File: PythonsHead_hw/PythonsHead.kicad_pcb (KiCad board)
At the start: 2 copper layers, 45 x 45 mm, 92 parts, among them Q1 MMBT2222, Q2 MMBT2222, Q3 MMBT2222, Q4 MMBT2222, Q5 MMBT2222, Q6 MMBT2222, Q7 MMBT2222, Q8 MMBT2222

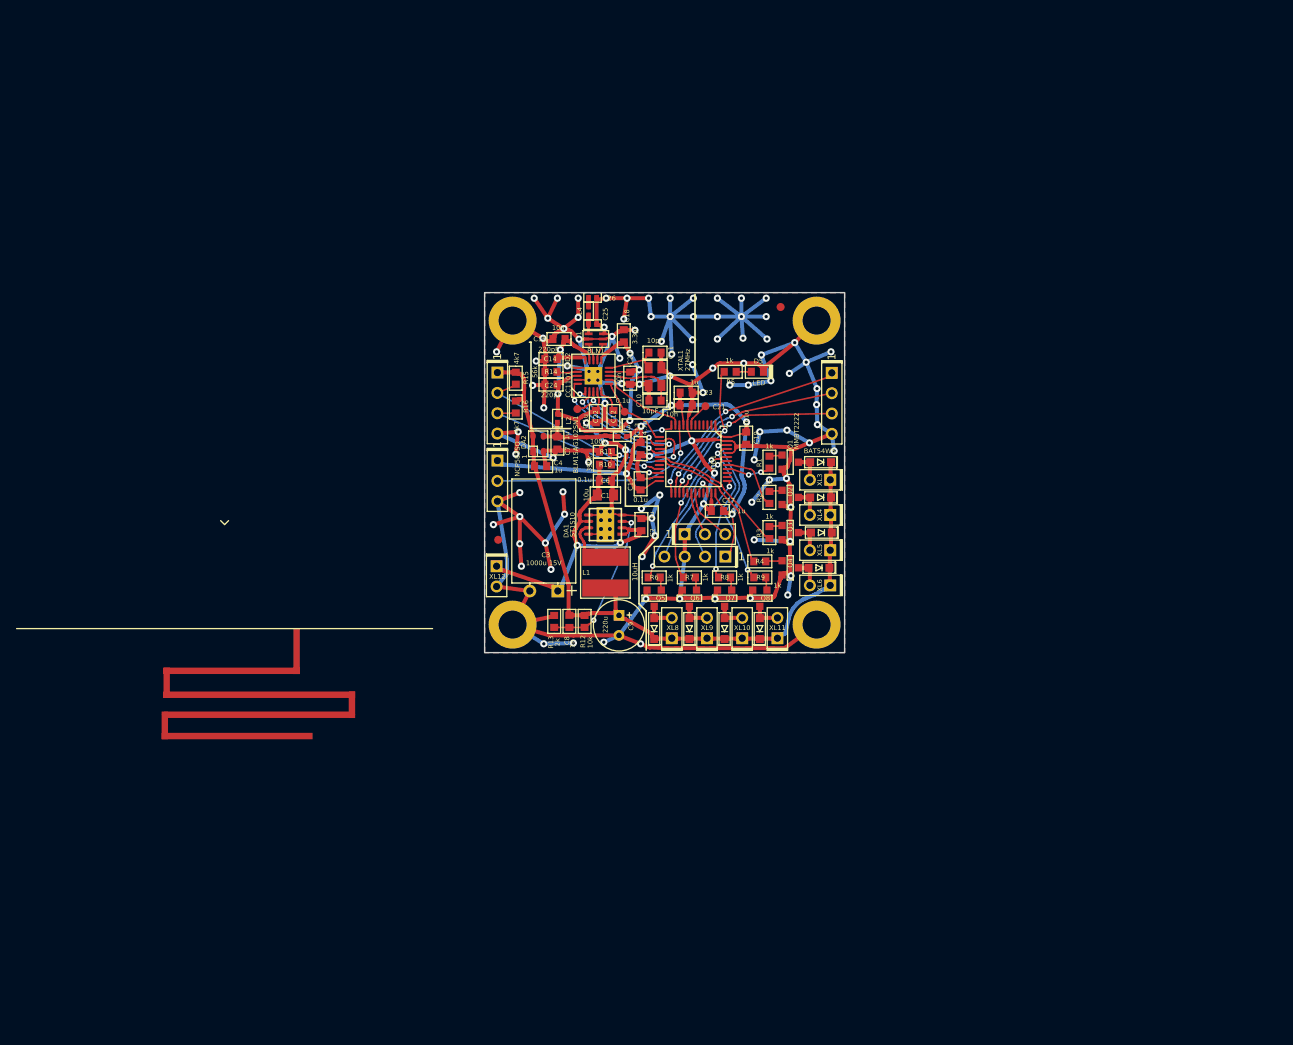
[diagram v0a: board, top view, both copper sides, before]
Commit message: * HW done + FW radio init
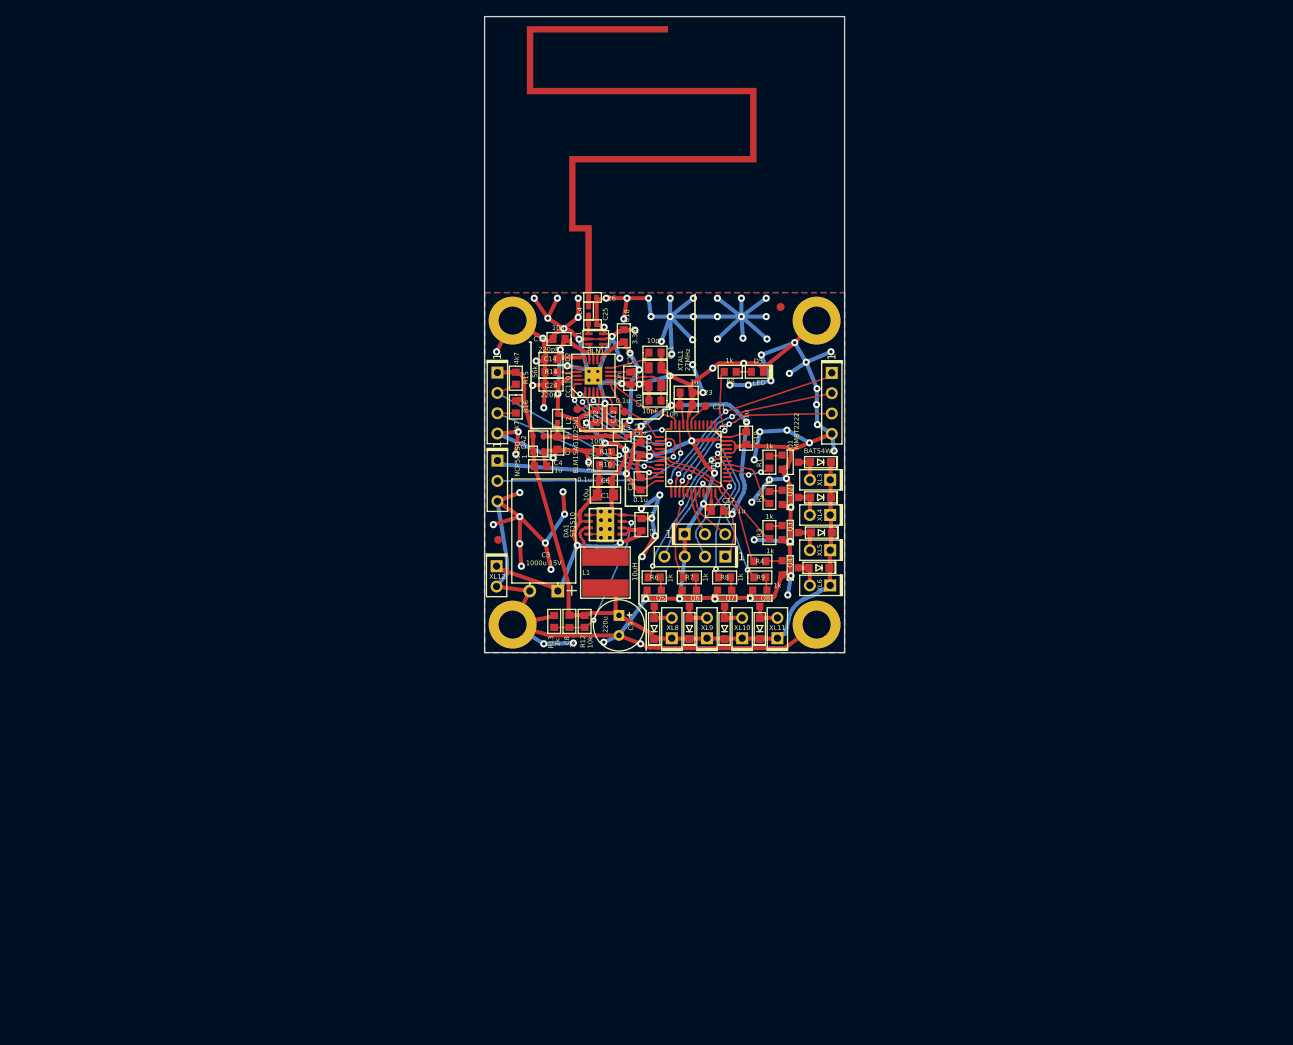
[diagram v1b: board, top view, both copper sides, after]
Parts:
- ANT1: footprint Radio:ANT_868_ROUND_MEANDER -> Radio:ANT_868_MEANDER_4HOR_45mm
- moved ANT1 69.2 mm to (114.5, 54.0), turned to 180 degrees
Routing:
- net /ANT2: track 1.20 -> 6.02 mm
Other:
- board size 45 x 45 mm -> 45 x 79.5 mm
- net class Ant added: clearance 0.2, trace_width 0.6, via_dia 0.7, via_drill 0.3
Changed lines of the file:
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@@
   (general
     (links 214)
-    (no_connects 8)
-    (area 32.488919 52.655 137.97363 112.775001)
+    (no_connects 7)
+    (area 91.924999 53.924999 137.075001 99.075001)
     (thickness 1.6)
-    (drawings 28)
-    (tracks 2345)
+    (drawings 30)
+    (tracks 2346)
     (zones 0)
     (modules 92)
@@
   (page A4)
   (layers
-    (0 F.Cu signal hide)
-    (31 B.Cu signal hide)
+    (0 F.Cu signal)
+    (31 B.Cu signal)
     (36 B.SilkS user)
     (37 F.SilkS user)
@@
     (40 Dwgs.User user)
     (44 Edge.Cuts user)
+    (49 F.Fab user hide)
   )
   (setup
@@
     (uvia_dia 0.3)
     (uvia_drill 0.1)
-    (add_net /ANT1)
-    (add_net /ANT2)
     (add_net /BAT_MEAS)
     (add_net /CC_CS)
@@
     (add_net "Net-(Q8-Pad1)")
   )
+  (net_class Ant ""
+    (clearance 0.2)
+    (trace_width 0.6)
+    (via_dia 0.7)
+    (via_drill 0.3)
+    (uvia_dia 0.3)
+    (uvia_drill 0.1)
+    (add_net /ANT1)
+    (add_net /ANT2)
+  )
   (net_class Wide ""
     (clearance 0.2)
@@
     (add_net VCC)
   )
-  (module Radio:ANT_868_ROUND_MEANDER (layer F.Cu)
-    (at 59.5 96)
-    (descr "Meander antenna for circular PCB R=29.5")
-    (fp_text reference ANT1 (at -7.4 1) (layer F.SilkS) hide
-      (effects (font (size 0.6 0.6) (thickness 0.15)))
-    )
-    (fp_text value ANT_PCB_MONO (at -8.2 2.6) (layer F.Fab) hide
-      (effects (font (size 0.6 0.6) (thickness 0.15)))
-    )
-    (fp_circle (center -20.5 2.5) (end -20.5 -0.5) (layer Dwgs.User) (width 0.15))
-    (fp_line (start 26 0) (end -26 0) (layer F.SilkS) (width 0.15))
-    (fp_arc (start 0 -13) (end 0 16.5) (angle 65) (layer Dwgs.User) (width 0.15))
-    (fp_arc (start 0 -13) (end 0 16.5) (angle -65) (layer Dwgs.User) (width 0.15))
-    (fp_line (start -0.5 -13.5) (end 0 -13) (layer F.SilkS) (width 0.15))
-    (fp_line (start 0.5 -13.5) (end 0 -13) (layer F.SilkS) (width 0.15))
-    (pad 1 smd rect (at 0.88 5.28 180) (size 17.04 0.8) (layers F.Cu)
-      (net 1 /ANT2))
-    (pad 1 smd rect (at -7.24 6.775 180) (size 0.8 3.79) (layers F.Cu)
-      (net 1 /ANT2))
-    (pad 1 smd rect (at 15.92 9.525 180) (size 0.8 3.31) (layers F.Cu)
-      (net 1 /ANT2))
-    (pad 1 smd rect (at 4.34 8.27 180) (size 23.96 0.8) (layers F.Cu)
-      (net 1 /ANT2))
-    (pad 1 smd rect (at 1.565 13.43 180) (size 18.87 0.8) (layers F.Cu)
-      (net 1 /ANT2))
-    (pad 1 smd oval (at 4.23 10.77 180) (size 24.18 0.8) (layers F.Cu)
-      (net 1 /ANT2))
-    (pad 1 smd rect (at -7.47 12.1 180) (size 0.8 3.46) (layers F.Cu)
-      (net 1 /ANT2))
-    (pad 1 smd rect (at 9 2.84 180) (size 0.8 5.68) (layers F.Cu)
-      (net 1 /ANT2))
-  )
   (module Radio:BALUN_JOHANSON868 (layer F.Cu)
     (at 105.9 59.8 90)
@@
     )
   )
+  (module Radio:ANT_868_MEANDER_4HOR_45mm (layer F.Cu)
+    (at 114.5 54 180)
+    (fp_text reference ANT1 (at 0 -2.5 180) (layer F.SilkS) hide
+      (effects (font (size 1 1) (thickness 0.15)))
+    )
+    (fp_text value ANT_PCB_MONO (at 0 -1 180) (layer F.SilkS) hide
+      (effects (font (size 1 1) (thickness 0.15)))
+    )
+    (fp_line (start -22.5 0) (end 22.5 0) (layer F.Fab) (width 0.15))
+    (fp_line (start 22.5 0) (end 22.5 34.5) (layer F.Fab) (width 0.15))
+    (fp_line (start 22.5 34.5) (end -22.5 34.5) (layer F.Fab) (width 0.15))
+    (fp_line (start -22.5 34.5) (end -22.5 0) (layer F.Fab) (width 0.15))
+    (pad 1 smd rect (at 9.5 4.215 180) (size 0.8 8.43) (layers F.Cu)
+      (net 1 /ANT2))
+    (pad 1 smd rect (at 10.515 8.03 180) (size 1.23 0.8) (layers F.Cu)
+      (net 1 /ANT2))
+    (pad 1 smd rect (at 11.53 12.35 180) (size 0.8 9.44) (layers F.Cu)
+      (net 1 /ANT2))
+    (pad 1 smd rect (at 0.22 16.67 180) (size 21.82 0.8) (layers F.Cu)
+      (net 1 /ANT2))
+    (pad 1 smd rect (at -11.09 20.93 180) (size 0.8 9.32) (layers F.Cu)
+      (net 1 /ANT2))
+    (pad 1 smd rect (at 2.865 25.19 180) (size 27.11 0.8) (layers F.Cu)
+      (net 1 /ANT2))
+    (pad 1 smd rect (at 16.82 29.045 180) (size 0.8 8.51) (layers F.Cu)
+      (net 1 /ANT2))
+    (pad 1 smd rect (at 8 32.91 180) (size 16.84 0.8) (layers F.Cu)
+      (net 1 /ANT2))
+  )
+  (gr_line (start 137 19.5) (end 137 54) (angle 90) (layer Edge.Cuts) (width 0.15))
+  (gr_line (start 92 19.5) (end 137 19.5) (angle 90) (layer Edge.Cuts) (width 0.15))
+  (gr_line (start 92 54) (end 92 19.5) (angle 90) (layer Edge.Cuts) (width 0.15))
   (gr_line (start 112.2 93.8) (end 112.2 98.7) (angle 90) (layer F.SilkS) (width 0.2))
   (gr_line (start 111.3 92.9) (end 112.2 93.8) (angle 90) (layer F.SilkS) (width 0.2))
@@
   (gr_line (start 137 99) (end 92 99) (angle 90) (layer Edge.Cuts) (width 0.15))
   (gr_line (start 137 54) (end 137 99) (angle 90) (layer Edge.Cuts) (width 0.15))
-  (gr_line (start 92 54) (end 137 54) (angle 90) (layer Edge.Cuts) (width 0.15))
+  (segment (start 105 54.6) (end 105 49.785) (width 0.6) (layer F.Cu) (net 1) (status C00000))
   (segment (start 105 54.9) (end 105 54.6) (width 0.6) (layer F.Cu) (net 1))
   (segment (start 105 55.5) (end 105 54.9) (width 0.6) (layer F.Cu) (net 1))
@@
   (segment (start 127.289 91.184) (end 127.2195 90.8268) (width 0.2) (layer F.Cu) (net 60))
   (zone (net 3) (net_name GND) (layer F.Cu) (hatch edge 0.508)
-    (connect_pads (clearance 0.3))
+    (connect_pads yes (clearance 0.3))
     (min_thickness 0.254)
     (fill yes (arc_segments 32) (thermal_gap 0.3) (thermal_bridge_width 0.3))
@@
   )
   (zone (net 3) (net_name GND) (layer B.Cu) (hatch edge 0.508)
-    (connect_pads (clearance 0.3))
+    (connect_pads yes (clearance 0.3))
     (min_thickness 0.254)
     (fill yes (arc_segments 32) (thermal_gap 0.3) (thermal_bridge_width 0.3))

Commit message: Layout done
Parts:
- removed C14: 220pF, Capacitors:CAP_0603
- removed XL13: CONN_3, Connectors:PLS-3
- added C27: 18pF, Capacitors:CAP_0603, F.Cu at (115.4, 85.0)
- added C28: 10n, Capacitors:CAP_0603, F.Cu at (105.4, 83.6)
- added C29: 0.1u, Capacitors:CAP_0603, F.Cu at (109.6, 93.2)
- added C30: 3.3pF, Capacitors:CAP_0603, F.Cu at (111.0, 83.6)
- added C31: 10n, Capacitors:CAP_0603, F.Cu at (113.0, 88.0)
- added C32: 0.1u, Capacitors:CAP_0603, F.Cu at (108.0, 93.2)
- added C33: 220pF, Capacitors:CAP_0603, F.Cu at (102.4, 88.8)
- added C34: *, Capacitors:CAP_0402, F.Cu at (105.8, 81.6)
- added C35: *, Capacitors:CAP_0402, F.Cu at (110.2, 81.6)
- added C36: 100u, Capacitors:SMD_D6d3, F.Cu at (95.0, 108.8)
- added C37: 100u, Capacitors:SMD_D6d3, F.Cu at (111.0, 108.8)
- added C38: 100u, Capacitors:SMD_D6d3, F.Cu at (103.0, 108.8)
- added C39: 100u, Capacitors:SMD_D6d3, F.Cu at (119.0, 108.8)
- added C40: 100u, Capacitors:SMD_D6d3, F.Cu at (94.6, 124.6)
- added C41: 100u, Capacitors:SMD_D6d3, F.Cu at (110.6, 124.6)
- added C42: 100u, Capacitors:SMD_D6d3, F.Cu at (102.6, 124.6)
- added C43: 100u, Capacitors:SMD_D6d3, F.Cu at (118.6, 124.6)
- added C44: 0.1u, Capacitors:CAP_0603, F.Cu at (94.6, 130.4)
- added C45: 0.1u, Capacitors:CAP_0603, F.Cu at (110.6, 130.4)
- added C46: 0.1u, Capacitors:CAP_0603, F.Cu at (102.6, 130.4)
- added C47: 0.1u, Capacitors:CAP_0603, F.Cu at (118.6, 130.4)
- added C48: 0.1u, Capacitors:CAP_0603, B.Cu at (96.6, 131.4)
- added C49: 0.1u, Capacitors:CAP_0603, B.Cu at (112.8, 131.4)
- added C5: 0.1u, Capacitors:CAP_0603, F.Cu at (82.8, 104.5)
- added C50: 0.1u, Capacitors:CAP_0603, B.Cu at (104.6, 131.4)
- added C51: 0.1u, Capacitors:CAP_0603, B.Cu at (120.8, 131.4)
- added C52: 100u, Capacitors:SMD_D6d3, F.Cu at (127.0, 108.8)
- added C53: 100u, Capacitors:SMD_D6d3, F.Cu at (143.0, 108.8)
- added C54: 100u, Capacitors:SMD_D6d3, F.Cu at (135.0, 108.8)
- added C55: 100u, Capacitors:SMD_D6d3, F.Cu at (151.0, 108.8)
- added C56: 100u, Capacitors:SMD_D6d3, F.Cu at (126.6, 124.6)
- added C57: 100u, Capacitors:SMD_D6d3, F.Cu at (142.6, 124.6)
- added C58: 100u, Capacitors:SMD_D6d3, F.Cu at (134.6, 124.6)
- added C59: 100u, Capacitors:SMD_D6d3, F.Cu at (150.6, 124.6)
- added C60: 0.1u, Capacitors:CAP_0603, F.Cu at (126.6, 130.4)
- added C61: 0.1u, Capacitors:CAP_0603, F.Cu at (142.6, 130.4)
- added C62: 0.1u, Capacitors:CAP_0603, F.Cu at (134.6, 130.4)
- added C63: 0.1u, Capacitors:CAP_0603, F.Cu at (150.6, 130.4)
- added C64: 0.1u, Capacitors:CAP_0603, B.Cu at (128.8, 131.4)
- added C65: 0.1u, Capacitors:CAP_0603, B.Cu at (144.8, 131.4)
- added C66: 0.1u, Capacitors:CAP_0603, B.Cu at (136.8, 131.4)
- added C67: 0.1u, Capacitors:CAP_0603, B.Cu at (152.8, 131.4)
- added DA10: AD8211, SOT:SOT23-5, B.Cu at (151.8, 135.6)
- added DA3: AD8211, SOT:SOT23-5, B.Cu at (95.8, 135.6)
- added DA4: AD8211, SOT:SOT23-5, B.Cu at (111.8, 135.6)
- added DA5: AD8211, SOT:SOT23-5, B.Cu at (103.8, 135.6)
- added DA6: AD8211, SOT:SOT23-5, B.Cu at (119.8, 135.6)
- added DA7: AD8211, SOT:SOT23-5, B.Cu at (127.8, 135.6)
- added DA8: AD8211, SOT:SOT23-5, B.Cu at (143.8, 135.6)
- added DA9: AD8211, SOT:SOT23-5, B.Cu at (135.8, 135.6)
- added DD3: CC1101, QFN_DFN:QFN20, F.Cu at (108.0, 87.8)
- added F1: Fuse0R, Resistors:RES_0603_FUSE, F.Cu at (80.5, 100.2)
- added L10: BLM15AG102, Inductors:IND_0402, B.Cu at (111.2, 131.8)
- added L11: BLM15AG102, Inductors:IND_0402, B.Cu at (103.0, 131.8)
- added L12: BLM15AG102, Inductors:IND_0402, B.Cu at (119.2, 131.8)
- added L13: 22uH, Inductors:SRN5040, F.Cu at (127.4, 118.0)
- added L14: 22uH, Inductors:SRN5040, F.Cu at (143.4, 118.0)
- added L15: 22uH, Inductors:SRN5040, F.Cu at (135.4, 118.0)
- added L16: 22uH, Inductors:SRN5040, F.Cu at (151.4, 118.0)
- added L17: BLM15AG102, Inductors:IND_0402, B.Cu at (127.2, 131.8)
- added L18: BLM15AG102, Inductors:IND_0402, B.Cu at (143.2, 131.8)
- added L19: BLM15AG102, Inductors:IND_0402, B.Cu at (135.2, 131.8)
- added L20: BLM15AG102, Inductors:IND_0402, B.Cu at (151.2, 131.8)
- added L5: 22uH, Inductors:SRN5040, F.Cu at (95.4, 118.0)
- added L6: 22uH, Inductors:SRN5040, F.Cu at (111.4, 118.0)
- added L7: 22uH, Inductors:SRN5040, F.Cu at (103.4, 118.0)
- added L8: 22uH, Inductors:SRN5040, F.Cu at (119.4, 118.0)
- added L9: BLM15AG102, Inductors:IND_0402, B.Cu at (95.0, 131.8)
- added Logo1: Logo, Pictures:Ostranna_16d9_13d5, F.Cu at (146.7, 72.7)
- added Q10: IRLML9303, SOT:SOT23-3, F.Cu at (108.4, 114.0)
- added Q11: IRLML9303, SOT:SOT23-3, F.Cu at (100.4, 114.0)
- added Q12: IRLML9303, SOT:SOT23-3, F.Cu at (116.4, 114.0)
- added Q13: IRLML6401, SOT:SOT23-3, F.Cu at (92.4, 133.2)
- added Q14: IRLML6244, SOT:SOT23-3, F.Cu at (92.4, 136.6)
- added Q15: IRLML6401, SOT:SOT23-3, F.Cu at (108.4, 133.2)
- added Q16: IRLML6244, SOT:SOT23-3, F.Cu at (108.4, 136.6)
- added Q17: IRLML6401, SOT:SOT23-3, F.Cu at (100.4, 133.2)
- added Q18: IRLML6244, SOT:SOT23-3, F.Cu at (100.4, 136.6)
- added Q19: IRLML6401, SOT:SOT23-3, F.Cu at (116.4, 133.2)
- added Q20: IRLML6244, SOT:SOT23-3, F.Cu at (116.4, 136.6)
- added Q21: IRLML6401, SOT:SOT23-3, F.Cu at (96.8, 133.2)
- added Q22: IRLML6244, SOT:SOT23-3, F.Cu at (96.8, 136.6)
- added Q23: IRLML6401, SOT:SOT23-3, F.Cu at (112.8, 133.2)
- added Q24: IRLML6244, SOT:SOT23-3, F.Cu at (112.8, 136.6)
- added Q25: IRLML6401, SOT:SOT23-3, F.Cu at (104.8, 133.2)
- added Q26: IRLML6244, SOT:SOT23-3, F.Cu at (104.8, 136.6)
- added Q27: IRLML6401, SOT:SOT23-3, F.Cu at (120.8, 133.2)
- added Q28: IRLML6244, SOT:SOT23-3, F.Cu at (120.8, 136.6)
- added Q29: IRLML9303, SOT:SOT23-3, F.Cu at (124.4, 114.0)
- added Q30: IRLML9303, SOT:SOT23-3, F.Cu at (140.4, 114.0)
- added Q31: IRLML9303, SOT:SOT23-3, F.Cu at (132.4, 114.0)
- added Q32: IRLML9303, SOT:SOT23-3, F.Cu at (148.4, 114.0)
- added Q33: IRLML6401, SOT:SOT23-3, F.Cu at (124.4, 133.3)
- added Q34: IRLML6244, SOT:SOT23-3, F.Cu at (124.4, 136.6)
- added Q35: IRLML6401, SOT:SOT23-3, F.Cu at (140.4, 133.3)
- added Q36: IRLML6244, SOT:SOT23-3, F.Cu at (140.4, 136.6)
- added Q37: IRLML6401, SOT:SOT23-3, F.Cu at (132.4, 133.3)
- added Q38: IRLML6244, SOT:SOT23-3, F.Cu at (132.4, 136.6)
- added Q39: IRLML6401, SOT:SOT23-3, F.Cu at (148.4, 133.3)
- added Q40: IRLML6244, SOT:SOT23-3, F.Cu at (148.4, 136.6)
- added Q41: IRLML6401, SOT:SOT23-3, F.Cu at (128.8, 133.3)
- added Q42: IRLML6244, SOT:SOT23-3, F.Cu at (128.8, 136.6)
- added Q43: IRLML6401, SOT:SOT23-3, F.Cu at (144.8, 133.3)
- added Q44: IRLML6244, SOT:SOT23-3, F.Cu at (144.8, 136.6)
- added Q45: IRLML6401, SOT:SOT23-3, F.Cu at (136.8, 133.3)
- added Q46: IRLML6244, SOT:SOT23-3, F.Cu at (136.8, 136.6)
- added Q47: IRLML6401, SOT:SOT23-3, F.Cu at (152.8, 133.3)
- added Q48: IRLML6244, SOT:SOT23-3, F.Cu at (152.8, 136.6)
- added Q9: IRLML9303, SOT:SOT23-3, F.Cu at (92.4, 114.0)
- added R17: 56k, Resistors:RES_0603, F.Cu at (88.1, 122.3)
- added R18: 56k, Resistors:RES_0603, F.Cu at (102.4, 87.2)
- added R19: 56k, Resistors:RES_0603, F.Cu at (96.8, 114.0)
- added R20: 56k, Resistors:RES_0603, F.Cu at (112.8, 114.0)
- added R21: 56k, Resistors:RES_0603, F.Cu at (104.8, 114.0)
- added R22: 56k, Resistors:RES_0603, F.Cu at (120.8, 114.0)
- added R23: 56k, Resistors:RES_0603, F.Cu at (92.0, 129.8)
- added R24: 56k, Resistors:RES_0603, F.Cu at (108.0, 129.8)
- added R25: 56k, Resistors:RES_0603, F.Cu at (100.0, 129.8)
- added R26: 56k, Resistors:RES_0603, F.Cu at (116.0, 129.8)
- added R27: 0R1, Resistors:RES_1206, B.Cu at (92.6, 135.6)
- added R28: 0R1, Resistors:RES_1206, B.Cu at (108.6, 135.6)
- added R29: 0R1, Resistors:RES_1206, B.Cu at (100.7, 135.6)
- added R30: 0R1, Resistors:RES_1206, B.Cu at (116.6, 135.6)
- added R31: 56k, Resistors:RES_0603, F.Cu at (97.2, 129.8)
- added R32: 56k, Resistors:RES_0603, F.Cu at (113.2, 129.8)
- added R33: 56k, Resistors:RES_0603, F.Cu at (105.2, 129.8)
- added R34: 56k, Resistors:RES_0603, F.Cu at (121.2, 129.8)
- added R35: 56k, Resistors:RES_0603, F.Cu at (128.8, 114.0)
- added R36: 56k, Resistors:RES_0603, F.Cu at (144.8, 114.0)
- added R37: 56k, Resistors:RES_0603, F.Cu at (136.8, 114.0)
- added R38: 56k, Resistors:RES_0603, F.Cu at (152.8, 114.0)
- added R39: 56k, Resistors:RES_0603, F.Cu at (124.0, 129.8)
- added R40: 56k, Resistors:RES_0603, F.Cu at (140.0, 129.8)
- added R41: 56k, Resistors:RES_0603, F.Cu at (132.0, 129.8)
- added R42: 56k, Resistors:RES_0603, F.Cu at (148.0, 129.8)
- added R43: 0R1, Resistors:RES_1206, B.Cu at (124.6, 135.6)
- added R44: 0R1, Resistors:RES_1206, B.Cu at (140.6, 135.6)
- added R45: 0R1, Resistors:RES_1206, B.Cu at (132.6, 135.6)
- added R46: 0R1, Resistors:RES_1206, B.Cu at (148.6, 135.6)
- added R47: 56k, Resistors:RES_0603, F.Cu at (129.2, 129.8)
- added R48: 56k, Resistors:RES_0603, F.Cu at (145.2, 129.8)
- added R49: 56k, Resistors:RES_0603, F.Cu at (137.2, 129.8)
- added R50: 56k, Resistors:RES_0603, F.Cu at (153.2, 129.8)
- added TP4: TESTPOINT, PCB:TESTPOINT_1MM, F.Cu at (115.4, 100.0)
- added TP5: TESTPOINT, PCB:TESTPOINT_1MM, F.Cu at (117.2, 100.0)
- added TP6: TESTPOINT, PCB:TESTPOINT_1MM, F.Cu at (120.8, 100.0)
- added TP7: TESTPOINT, PCB:TESTPOINT_1MM, F.Cu at (119.0, 100.0)
- added TP8: TESTPOINT, PCB:TESTPOINT_1MM, F.Cu at (122.6, 100.0)
- added XTAL2: 27MHz, Quartz:03225C4, F.Cu at (115.4, 88.0)
- ANT1: footprint Radio:ANT_868_MEANDER_4HOR_45mm -> Radio:ANT_868_ARMLETG
- BLN1: value 0896BM15A0001 -> BALUN868JOHANSON
- C1: value 10u -> 0.1u; footprint Capacitors:CAP_0805 -> Capacitors:CAP_0603
- C10, C11: value 10pF -> 0.1u
- C12: value 0.1u -> 10u
- C13: value 4.7u -> 0.1u
- C16, C20: value 10n -> 0.1u
- C18: value 3.3pF -> 0.1u
- C2: value 1u -> 100u; footprint Capacitors:CAP_0603 -> Capacitors:SMD_D6d3
- C21: value 10n -> 1u
- C24: value 220pF -> 0.1u
- C25: value 1.5pF -> 18pF; footprint Capacitors:CAP_0402 -> Capacitors:CAP_0603
- C26: value DoNotMount -> 220pF; footprint Capacitors:CAP_0402 -> Capacitors:CAP_0603
- C3: value 1000u 15V -> 10u; footprint Capacitors:CAP_08xxR_HOR -> Capacitors:CAP_0805
- C4: value 1u -> 18pF
- C6: value 0.1u -> 18pF
- C7: value 1u -> 10u
- C8: value 1n -> 2u2
- C9: value 220u -> 2u2; footprint Capacitors:CAP_06xxR -> Capacitors:CAP_0603
- D1: value BAT54WS -> LED; footprint Diodes:SOD323 -> LEDs:LED_0603
- D2, D3, D4, D6, D7, D8, D9: value BAT54WS -> PMEG2020
- D5: value LED -> PMEG2020; footprint LEDs:LED_0603 -> Diodes:SOD323
- DA1: value ST1S10 -> LD1117; footprint QFN_DFN:DFN8 -> SOT:SOT223
- DA2: value NCP583SQ -> NCP662SQ
- DD1: value STM32L151CxTx -> 24C08; footprint LQFP_TQFP:LQFP48 -> SO_DIL_TSSOP:SO8_150MIL
- DD2: value CC1101 -> STM32F205VX-100; footprint QFN_DFN:QFN20 -> LQFP_TQFP:LQFP100
- HOLE1, HOLE2, HOLE3, HOLE4: footprint PCB:Hole3_5_out6mm -> PCB:Hole2d4_out4d5mm
- L1: value 10uH -> BLM15AG102; footprint Inductors:IND_SDR0604 -> Inductors:IND_0402
- L2, L3: value BLM15AG102SN1 -> BLM15AG102
- L4: value 5.6nH -> *
- Q1, Q2, Q3, Q4, Q5, Q6, Q7, Q8: value MMBT2222 -> IRLML9303
- R1, R2: value 1k -> 10k
- R10: value 390k -> 51R
- R11: value 100k -> 510R
- R12: value 10k -> 510R
- R13: value 2k -> 510R
- R14: value 56k -> 510R
- R15: value 4k7 -> 100k
- R3: value 1k -> 4k7
- R5: value 1k -> 390R
- R6, R7, R8, R9: value 1k -> 510R
- XL1: value CONN_3 -> CONN_6; footprint Connectors:PLS-3 -> Connectors:PLS-6
- XL10, XL11, XL12, XL5, XL6, XL8, XL9: footprint Connectors:PLS-2 -> Connectors:W02_Pitch_2d54
- XL14: footprint Connectors:PLS-4 -> Connectors:WB-04(MW-4M)
- XL2: value ST_SWD -> CONN_2; footprint Connectors:PLS-4 -> Connectors:PWL2-02
- XL3, XL4: value CONN_2 -> CONN_5; footprint Connectors:PLS-2 -> Connectors:WB-05R(MW-5MR)
- XL7: value CONN_4 -> CONN_2; footprint Connectors:PLS-4 -> Connectors:W02_Pitch_2d54
- XTAL1: value 27MHz -> 12MHz; footprint Quartz:03225C4 -> Quartz:0503x4-4
- moved HOLE1 102.6 mm to (164.2, 133.7)
- moved RP1 91.2 mm to (165.2, 141.5)
- moved XL14 90.2 mm to (164.6, 119.7), turned to 90 degrees
- moved R14 90.2 mm to (155.6, 135.1), turned to 90 degrees
- moved XL7 84.8 mm to (102.6, 142.2), turned to 0 degrees
- moved R16 81.6 mm to (160.1, 118.7), turned to 0 degrees
- moved R11 81.2 mm to (160.4, 135.1), turned to 90 degrees
- moved XL3 79.6 mm to (84.4, 138.7)
- moved XL12 78.6 mm to (150.6, 142.2), turned to 0 degrees
- moved R13 69.2 mm to (157.2, 135.1)
- moved XL5 69.2 mm to (94.6, 142.2), turned to 0 degrees
- moved Q1 69.2 mm to (88.8, 130.6), turned to 270 degrees
- moved R12 67.4 mm to (158.8, 135.1), turned to 90 degrees
- moved Q3 65.1 mm to (84.8, 130.6), turned to 270 degrees
- moved HOLE3 64.9 mm to (81.0, 133.7)
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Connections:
- C1 pad 1: +BATT -> GND
- C1 pad 2: GND -> PwrMCU
- C10 pad 1: Net-(C10-Pad1) -> GND
- C10 pad 2: GND -> +5V
- C11 pad 1: Net-(C11-Pad1) -> GND
- C11 pad 2: GND -> PwrMCU
- C12 pad 1: Net-(C12-Pad1) -> GND
- C12 pad 2: GND -> +5V
- C13 pad 1: PwrMCU -> GND
- C13 pad 2: GND -> PwrMCU
- C15 pad 1: PwrMCU -> GND
- C15 pad 2: GND -> PwrMCU
- C16 pad 1: VCC -> GND
- C16 pad 2: GND -> PwrMCU
- C17 pad 1: PwrMCU -> +5V
- C18 pad 1: VCC -> GND
- C18 pad 2: GND -> PwrMCU
- C19 pad 1: PwrMCU -> GND
- C19 pad 2: GND -> PwrMCU
- C2 pad 2: GND -> GNDPWR
- C20 pad 1: VCC -> GND
- C20 pad 2: GND -> PwrMCU
- C21 pad 1: PwrMCU -> +3.3V
- C22 pad 1: VCC -> GND
- C22 pad 2: GND -> /VDDA
- C23 pad 1: PwrMCU -> GND
- C23 pad 2: GND -> /VDDA
- C24 pad 1: VCC -> GND
- C24 pad 2: GND -> /Vref+
- C25 pad 1: /ANT1 -> Net-(C25-Pad1)
- C26 pad 1: /ANT2 -> GND
- C26 pad 2: GND -> VCC
- C3 pad 2: GND -> GNDPWR
- C4 pad 1: +5V -> Net-(C4-Pad1)
- C6 pad 1: GND -> Net-(C6-Pad1)
- C6 pad 2: +BATT -> GND
- C7 pad 1: +3.3V -> GND
- C7 pad 2: GND -> PwrMCU
- C8 pad 1: +5V -> Net-(C8-Pad1)
- C8 pad 2: Net-(C8-Pad2) -> GND
- C9 pad 1: +5V -> Net-(C9-Pad1)
- D1 pad A: /PWM1_OUT -> Net-(D1-PadA)
- D1 pad C: +5V -> GND
- D2 pad A: /PWM2_OUT -> GNDPWR
- D2 pad C: +5V -> Net-(D2-PadC)
- D3 pad A: /PWM3_OUT -> GNDPWR
- D3 pad C: +5V -> Net-(D3-PadC)
- D4 pad A: /PWM4_OUT -> GNDPWR
- D4 pad C: +5V -> Net-(D4-PadC)
- D5 pad A: Net-(D5-PadA) -> GNDPWR
- D5 pad C: GND -> Net-(D5-PadC)
- D6 pad A: /PWM5_OUT -> GNDPWR
- D6 pad C: +5V -> Net-(D6-PadC)
- D7 pad A: /PWM6_OUT -> GNDPWR
- D7 pad C: +5V -> Net-(D7-PadC)
- D8 pad A: /PWM7_OUT -> GNDPWR
- D8 pad C: +5V -> Net-(D8-PadC)
- D9 pad A: /PWM8_OUT -> GNDPWR
- D9 pad C: +5V -> Net-(D9-PadC)
- DA1 pad 1: +BATT -> GND
- DA1 pad 2: +BATT -> +5V
- DA1 pad 3: Net-(C8-Pad2) -> +BATT
- DA1 pad PAD: GND -> +5V
- DA2 pad 1: +5V -> GND
- DA2 pad 2: GND -> +5V
- DD1 pad 1: PwrMCU -> GND
- DD1 pad 2: (no net) -> GND
- DD1 pad 3: (no net) -> GND
- DD1 pad 4: (no net) -> GND
- DD1 pad 5: (no net) -> /SDA_EE
- DD1 pad 6: (no net) -> /SCL_EE
- DD1 pad 7: Net-(DD1-Pad7) -> GND
- DD1 pad 8: GND -> PwrMCU
- DD2 pad 1: /CC_SCK -> (no net)
- DD2 pad 10: Net-(C11-Pad1) -> GND
- DD2 pad 11: VCC -> PwrMCU
- DD2 pad 12: /RF1 -> Net-(C4-Pad1)
- DD2 pad 13: /RF2 -> Net-(DD2-Pad13)
- DD2 pad 14: VCC -> (no net)
- DD2 pad 15: VCC -> /HTRD_CURR
- DD2 pad 16: GND -> /HTRE_CURR
- DD2 pad 17: Net-(DD2-Pad17) -> /HTRF_CURR
- DD2 pad 18: VCC -> /HTRG_CURR
- DD2 pad 19: GND -> PwrMCU
- DD2 pad 2: /CC_MISO -> (no net)
- DD2 pad 20: /CC_MOSI -> GND
- DD2 pad 3: /CC_GDO2 -> (no net)
- DD2 pad 4: VCC -> (no net)
- DD2 pad 5: Net-(C12-Pad1) -> (no net)
- DD2 pad 6: /CC_GDO0 -> PwrMCU
- DD2 pad 7: /CC_CS -> (no net)
- DD2 pad 8: Net-(C10-Pad1) -> (no net)
- DD2 pad 9: VCC -> (no net)
- L1 pad 1: +5V -> PwrMCU
- L1 pad 2: Net-(DA1-Pad7) -> +3.3V
- L2 pad 1: VCC -> /VDDA
- L2 pad 2: +3.3V -> PwrMCU
- L3 pad 1: PwrMCU -> VCC
- Q1 pad 1: Net-(Q1-Pad1) -> /LED1_PWM_CTRL
- Q1 pad 2: GND -> +5V
- Q1 pad 3: /PWM1_OUT -> Net-(Q1-Pad3)
- Q2 pad 1: Net-(Q2-Pad1) -> /LED2_PWM_CTRL
- Q2 pad 2: GND -> +5V
- Q2 pad 3: /PWM2_OUT -> Net-(Q2-Pad3)
- Q3 pad 1: Net-(Q3-Pad1) -> /LED3_PWM_CTRL
- Q3 pad 2: GND -> +5V
- Q3 pad 3: /PWM3_OUT -> Net-(Q3-Pad3)
- Q4 pad 1: Net-(Q4-Pad1) -> /LED4_PWM_CTRL
- Q4 pad 2: GND -> +5V
- Q4 pad 3: /PWM4_OUT -> Net-(Q4-Pad3)
- Q5 pad 1: Net-(Q5-Pad1) -> /LED5_PWM_CTRL
- Q5 pad 2: GND -> +5V
- Q5 pad 3: /PWM5_OUT -> Net-(Q5-Pad3)
- Q6 pad 1: Net-(Q6-Pad1) -> /LED6_PWM_CTRL
- Q6 pad 2: GND -> +5V
- Q6 pad 3: /PWM6_OUT -> Net-(Q6-Pad3)
- Q7 pad 1: Net-(Q7-Pad1) -> /LED7_PWM_CTRL
- Q7 pad 2: GND -> +5V
- Q7 pad 3: /PWM7_OUT -> Net-(Q7-Pad3)
- Q8 pad 1: Net-(Q8-Pad1) -> /LED8_PWM_CTRL
- Q8 pad 2: GND -> +5V
- Q8 pad 3: /PWM8_OUT -> Net-(Q8-Pad3)
- R1 pad 1: /PWM1 -> PwrMCU
- R1 pad 2: Net-(Q1-Pad1) -> /SDA_EE
- R10 pad 1: +BATT -> /Vref+
- R10 pad 2: /BAT_MEAS -> /VDDA
- R11 pad 1: /BAT_MEAS -> Net-(R11-Pad1)
- R11 pad 2: GND -> Net-(Q5-Pad3)
- R12 pad 1: +5V -> Net-(R12-Pad1)
- R12 pad 2: Net-(C8-Pad2) -> Net-(Q6-Pad3)
- R13 pad 1: Net-(C8-Pad2) -> Net-(R13-Pad1)
- R13 pad 2: GND -> Net-(Q7-Pad3)
- R14 pad 1: Net-(DD2-Pad17) -> Net-(R14-Pad1)
- R14 pad 2: GND -> Net-(Q8-Pad3)
- R15 pad 1: +5V -> +BATT
- R15 pad 2: /I2C_SCL -> /BAT_MEAS
- R16 pad 2: /I2C_SDA -> /SDA_SNS
- R2 pad 1: /PWM2 -> /SCL_EE
- R2 pad 2: Net-(Q2-Pad1) -> PwrMCU
- R3 pad 1: /PWM3 -> +5V
- R3 pad 2: Net-(Q3-Pad1) -> /SCL_SNS
- R4 pad 1: /PWM4 -> Net-(D1-PadA)
- R4 pad 2: Net-(Q4-Pad1) -> /LED
- R5 pad 1: Net-(D5-PadA) -> Net-(DD2-Pad13)
- R5 pad 2: Net-(DD1-Pad28) -> Net-(C6-Pad1)
- R6 pad 1: /PWM5 -> Net-(R6-Pad1)
- R6 pad 2: Net-(Q5-Pad1) -> Net-(Q1-Pad3)
- R7 pad 1: /PWM6 -> Net-(R7-Pad1)
- R7 pad 2: Net-(Q6-Pad1) -> Net-(Q2-Pad3)
- R8 pad 1: /PWM7 -> Net-(R8-Pad1)
- R8 pad 2: Net-(Q7-Pad1) -> Net-(Q3-Pad3)
- R9 pad 1: /PWM8 -> Net-(R9-Pad1)
- R9 pad 2: Net-(Q8-Pad1) -> Net-(Q4-Pad3)
- TP1 pad 1: Net-(DD1-Pad7) -> /HTRA_CURR
- TP2 pad 1: /CC_GDO0 -> /HTRC_CURR
- TP3 pad 1: /CC_GDO2 -> /HTRB_CURR
- XL1 pad 1: GND -> PwrMCU
- XL1 pad 2: /UART_TX -> /SWCLK
- XL1 pad 3: /UART_RX -> GND
- XL10 pad 1: +5V -> /HTRG1
- XL10 pad 2: /PWM7_OUT -> /HTRG2
- XL11 pad 1: +5V -> /HTRF1
- XL11 pad 2: /PWM8_OUT -> /HTRF2
- XL12 pad 1: +BATT -> /HTRH1
- XL12 pad 2: GND -> /HTRH2
- XL14 pad 2: /I2C_SCL -> /SCL_SNS
- XL14 pad 3: /I2C_SDA -> /SDA_SNS
- XL2 pad 1: PwrMCU -> GNDPWR
- XL2 pad 2: /SWCLK -> +BATT
- XL3 pad 1: +5V -> GND
- XL3 pad 2: /PWM1_OUT -> Net-(R6-Pad1)
- XL4 pad 1: +5V -> GND
- XL4 pad 2: /PWM2_OUT -> Net-(R11-Pad1)
- XL5 pad 1: +5V -> /HTRA1
- XL5 pad 2: /PWM3_OUT -> /HTRA2
- XL6 pad 1: +5V -> /HTRC1
- XL6 pad 2: /PWM4_OUT -> /HTRC2
- XL7 pad 1: Net-(DD1-Pad25) -> /HTRB1
- XL7 pad 2: Net-(DD1-Pad26) -> /HTRB2
- XL8 pad 1: +5V -> /HTRD1
- XL8 pad 2: /PWM5_OUT -> /HTRD2
- XL9 pad 1: +5V -> /HTRE1
- XL9 pad 2: /PWM6_OUT -> /HTRE2
- XTAL1 pad 1: Net-(C10-Pad1) -> Net-(C4-Pad1)
- XTAL1 pad 2: Net-(C11-Pad1) -> Net-(C6-Pad1)
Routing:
- net GND: track 536.4 -> 0.00 mm, vias 103 -> 0
- net +5V: track 92.4 -> 0.00 mm
- net PwrMCU: track 78.7 -> 0.00 mm, vias 5 -> 0
- net VCC: track 59.8 -> 0.00 mm, vias 5 -> 0
- net +BATT: track 41.6 -> 0.00 mm, vias 2 -> 0
- net Net-(DD1-Pad10): track 27.8 -> 0.00 mm, vias 1 -> 0
- net Net-(DD1-Pad25): track 27.0 -> 0.00 mm, vias 2 -> 0
- net Net-(DD1-Pad26): track 25.3 -> 0.00 mm, vias 2 -> 0
- net /I2C_SCL: track 25.2 -> 0.00 mm, vias 1 -> 0
- net Net-(DD1-Pad27): track 24.2 -> 0.00 mm, vias 2 -> 0
- net /I2C_SDA: track 24.0 -> 0.00 mm, vias 1 -> 0
- net /PWM8: track 19.7 -> 0.00 mm, vias 2 -> 0
- net Net-(C8-Pad2): track 19.5 -> 0.00 mm, vias 2 -> 0
- net /PWM4: track 18.8 -> 0.00 mm
- net /PWM5: track 18.4 -> 0.00 mm, vias 2 -> 0
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- removed copper zone on B.Cu, net GND
- removed copper zone on F.Cu, net GND
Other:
- board size 45 x 79.5 mm -> 88.4 x 78.7 mm
- board text added: "Ostranna"

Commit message: sent to fabric
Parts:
- added C14: 10u, Capacitors:CAP_0805, F.Cu at (86.6, 88.4)
- added C68: 10u, Capacitors:CAP_0805, F.Cu at (84.6, 88.4)
- added C69: 22n, Capacitors:CAP_0603, F.Cu at (81.2, 88.8)
- added C70: 0.1u, Capacitors:CAP_0603, F.Cu at (82.8, 88.8)
- added C71: 1u, Capacitors:CAP_0603, F.Cu at (85.8, 92.4)
- added C72: 0.47u, Capacitors:CAP_0603, F.Cu at (87.5, 106.9)
- added C73: 470pF, Capacitors:CAP_0603, F.Cu at (94.4, 88.4)
- added C75: 0.1u, Capacitors:CAP_0603, F.Cu at (96.4, 88.4)
- added DA11: LM3150, SO_DIL_TSSOP:HTSSOP14, F.Cu at (82.0, 95.8)
- added L21: 4.7uH, Inductors:13x13, F.Cu at (94.8, 97.0)
- added Q49: IRF8313, SO_DIL_TSSOP:SO8_150MIL, F.Cu at (83.8, 105.0)
- added R51: 100k, Resistors:RES_0603, F.Cu at (79.6, 88.8)
- added R52: 1k5, Resistors:RES_0603, F.Cu at (79.8, 102.4)
- added R53: 75k, Resistors:RES_0603, F.Cu at (91.4, 88.4)
- added R54: 10k, Resistors:RES_0603, F.Cu at (95.2, 85.7)
- C10, C12, C5, DA1, F1: moved to B.Cu
- moved C17 26.0 mm to (106.8, 102.4)
- moved C21 26.0 mm to (106.8, 97.2)
- moved DA2 26.0 mm to (106.8, 99.8)
- moved C12 17.9 mm to (96.5, 105.3)
- moved C10 15.9 mm to (96.5, 103.5)
- moved C5 13.1 mm to (93.4, 96.8), turned to 90 degrees
- moved F1 12.9 mm to (93.4, 100.2), turned to 90 degrees
- moved DA1 12.8 mm to (99.6, 98.6), turned to 90 degrees
- moved Q6 3.90 mm to (160.4, 130.6)
- moved Q5 3.80 mm to (160.4, 126.8)
- moved C3 2.91 mm to (80.0, 107.2), turned to 270 degrees
- moved R10 1.70 mm to (128.8, 98.4)
- moved L11 1.70 mm to (104.2, 130.6), turned to 0 degrees
- moved XL2 1.60 mm to (82.6, 119.9)
- moved C2 1.60 mm to (82.7, 112.6)
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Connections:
- C36 pad 1: +BATT -> VAA
- C37 pad 1: +BATT -> VAA
- C38 pad 1: +BATT -> VAA
- C39 pad 1: +BATT -> VAA
- C52 pad 1: +BATT -> VAA
- C53 pad 1: +BATT -> VAA
- C54 pad 1: +BATT -> VAA
- C55 pad 1: +BATT -> VAA
- Q10 pad 2: +BATT -> VAA
- Q11 pad 2: +BATT -> VAA
- Q12 pad 2: +BATT -> VAA
- Q29 pad 2: +BATT -> VAA
- Q30 pad 2: +BATT -> VAA
- Q31 pad 2: +BATT -> VAA
- Q32 pad 2: +BATT -> VAA
- Q9 pad 2: +BATT -> VAA
- R19 pad 1: +BATT -> VAA
- R20 pad 1: +BATT -> VAA
- R21 pad 1: +BATT -> VAA
- R22 pad 1: +BATT -> VAA
- R35 pad 1: +BATT -> VAA
- R36 pad 1: +BATT -> VAA
- R37 pad 1: +BATT -> VAA
- R38 pad 1: +BATT -> VAA
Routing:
- net GNDPWR: track 0.00 -> 574.9 mm, vias 0 -> 61
- net GND: track 0.00 -> 560.4 mm, vias 0 -> 44
- net +5V: track 0.00 -> 286.6 mm, vias 0 -> 19
- net PwrMCU: track 0.00 -> 137.3 mm, vias 0 -> 8
- net VAA: track 0.00 -> 125.9 mm
- net +BATT: track 0.00 -> 83.8 mm, vias 0 -> 2
- net /LED1_PWM_CTRL: track 0.00 -> 79.8 mm, vias 0 -> 2
- net /LED2_PWM_CTRL: track 0.00 -> 76.2 mm, vias 0 -> 2
- net /HTRH_CURR: track 0.00 -> 73.6 mm, vias 0 -> 3
- net /HTRE_DIR1: track 0.00 -> 73.4 mm, vias 0 -> 2
- net /HTRA_CURR: track 0.00 -> 70.4 mm, vias 0 -> 3
- net /HTRA_DIR1: track 0.00 -> 69.9 mm, vias 0 -> 2
- net /HTRB_DIR1: track 0.00 -> 67.8 mm, vias 0 -> 2
- net /HTRA_DIR2: track 0.00 -> 66.0 mm, vias 0 -> 2
- net /HTRF_DIR1: track 0.00 -> 65.5 mm, vias 0 -> 2
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- added copper zone on B.Cu, net GND
- added copper zone on F.Cu, net GND
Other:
- net class Ant removed
- net class Default: clearance 0.2 -> 0.22; trace_width 0.2 -> 0.22
- net class Wide: clearance 0.2 -> 0.22
- rule trace_clearance: 0.2 -> 0.22
- board text added: "A B C D E F G H"
- board text added: "Python v2"
